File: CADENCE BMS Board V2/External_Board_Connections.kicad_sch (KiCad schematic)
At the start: 42 parts, among them J10 Conn_01x08, J11 Conn_01x06, J12 Conn_01x02, J13 Conn_01x08, J14 Conn_01x04, J15 Conn_01x08, J2 Conn_01x02, J27 USB_C_Receptacle_USB2.0_16P, J3 Conn_01x08, J4 Conn_01x02, J5 Conn_01x01_Socket, J6 Conn_01x01_Socket, J7 Conn_01x01_Socket, J8 Conn_01x01_Socket, J9 Conn_01x04, Q27 Q_PMOS_DGS, Q28 Q_PMOS_DGS, U11 CYPD3177-24LQ

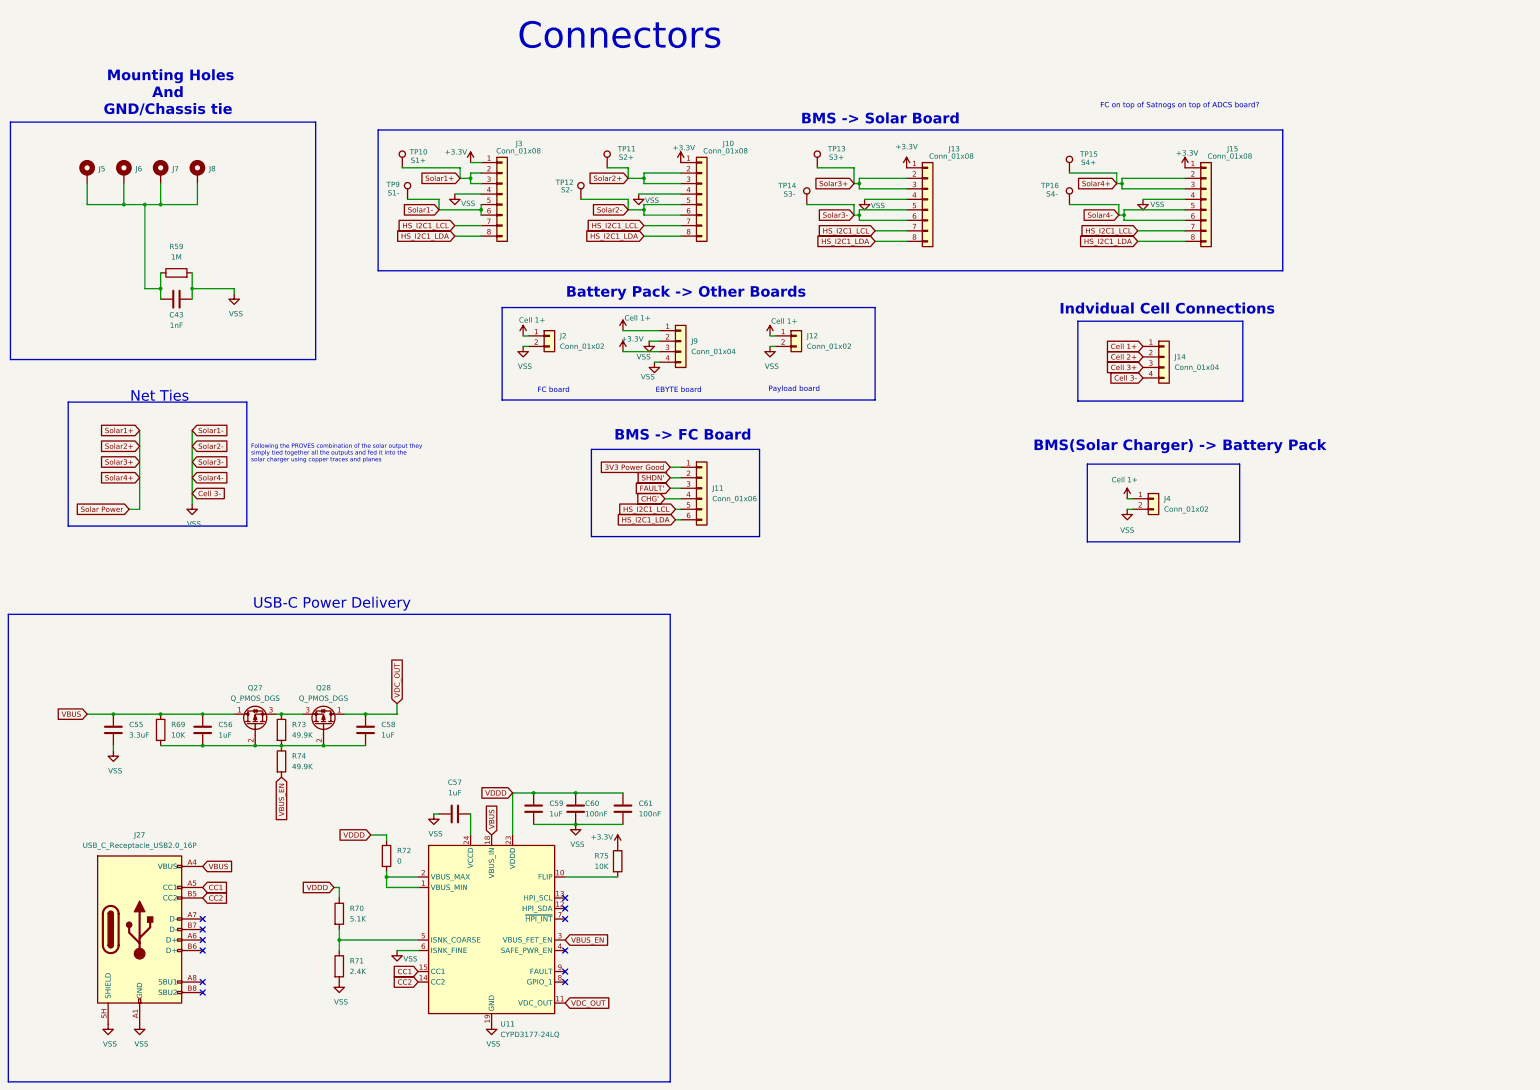
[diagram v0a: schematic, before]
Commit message: Adding in BMS V2 file for editing
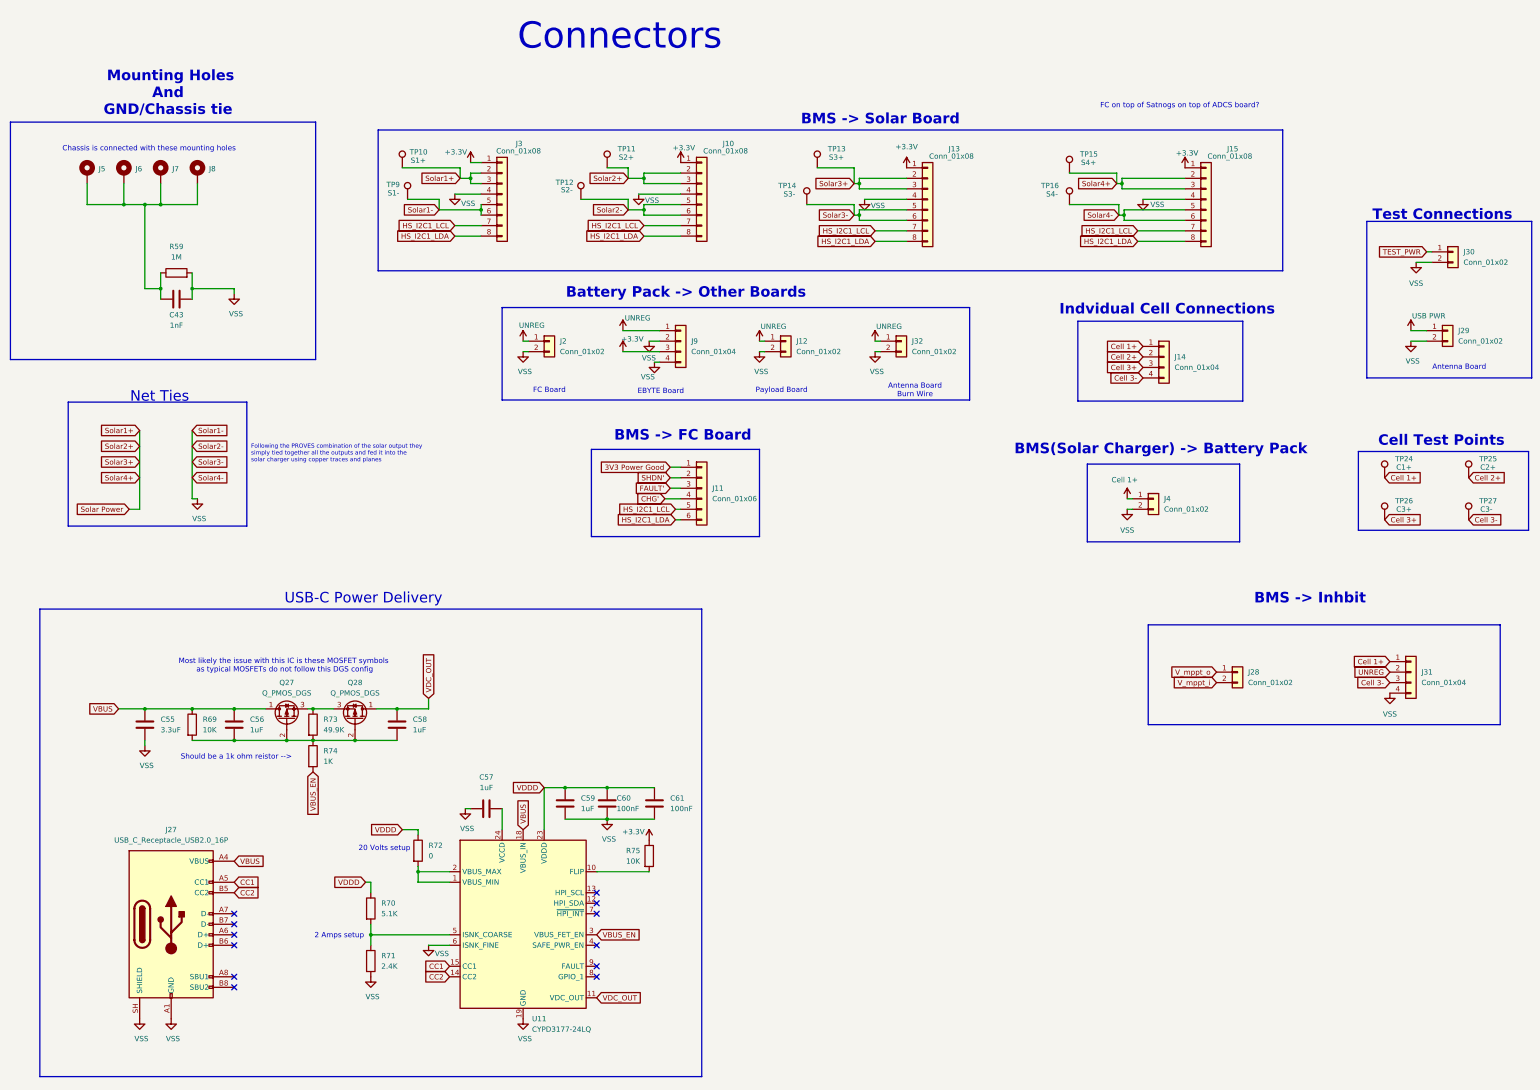
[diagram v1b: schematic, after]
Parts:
- added J28, J32: Conn_01x02, Connector_JST:JST_XH_B2B-XH-A_1x02_P2.50mm_Vertical, symbol Connector_Generic:Conn_01x02
- added J29, J30: Conn_01x02, JST_CON:SHDR2W120P580X500_2X1_790X1380X1460P, symbol Connector_Generic:Conn_01x02
- added J31: Conn_01x04, Connector_JST:JST_XH_B4B-XH-A_1x04_P2.50mm_Vertical, symbol Connector_Generic:Conn_01x04
- added TP24: C1+, TestPoint:TestPoint_THTPad_D1.0mm_Drill0.5mm, symbol Connector:TestPoint
- added TP25: C2+, TestPoint:TestPoint_THTPad_D1.0mm_Drill0.5mm, symbol Connector:TestPoint
- added TP26: C3+, TestPoint:TestPoint_THTPad_D1.0mm_Drill0.5mm, symbol Connector:TestPoint
- added TP27: C3-, TestPoint:TestPoint_THTPad_D1.0mm_Drill0.5mm, symbol Connector:TestPoint
- C43: footprint Diode_SMD:D_SOD-123 -> Capacitor_SMD:C_0805_2012Metric
- J14: footprint Connector_JST:JST_NV_B04P-NV_1x04_P5.00mm_Vertical -> JST_4Pin_CON:LC04T
- R74: value 49.9K -> 1K
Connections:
- net Cell 1+: now also J31.1 (Pin_1), TP24.1; no longer J12.1 (Pin_1), J2.1 (Pin_1), J9.1 (Pin_1)
- net Cell 2+: now also TP25.1
- net Cell 3+: now also TP26.1
- net VSS: now also J29.2 (Pin_2), J30.2 (Pin_2), J31.4 (Pin_4), J32.2 (Pin_2); no longer J14.4 (Pin_4)
- new net Cell 3-: J14.4 (Pin_4), J31.3 (Pin_3), TP27.1
- new net TEST_PWR: J30.1 (Pin_1)
- new net UNREG: J12.1 (Pin_1), J2.1 (Pin_1), J31.2 (Pin_2), J32.1 (Pin_1), J9.1 (Pin_1)
- new net USB PWR: J29.1 (Pin_1)
- new net V_mppt_i: J28.2 (Pin_2)
- new net V_mppt_o: J28.1 (Pin_1)
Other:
- note added: "2 Amps setup"
- note added: "20 Volts setup"
- note added: "Antenna Board"
- note added: "Antenna Board Burn Wire"
- note added: "BMS -> Inhbit"
- note added: "Cell Test Points"
- note added: "Chassis is connected with these mounting holes"
- note added: "EBYTE Board"
- note added: "FC Board"
- note added: "Most likely the issue with this IC is these MOSFET symbols as typical MOSFETs do not follow this DGS config"
- note added: "Payload Board"
- note added: "Should be a 1k ohm reistor -->"
- note added: "Test Connections"
- note removed: "EBYTE board"
- note removed: "FC board"
- note removed: "Payload board"
- moved on the sheet: J12, J2
